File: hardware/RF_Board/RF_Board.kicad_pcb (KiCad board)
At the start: 4 copper layers, 90 x 90 mm, 127 parts, among them J1 Conn_Coaxial, J2 Conn_01x07_Male, J3 Conn_Coaxial, J4 Conn_01x07_Male, J5 Conn_01x06_Female, J6 Conn_01x06_Female, J7 Conn_01x06_Female, J9 LD15S33E4GX00LF, Q1 2N7002, Q2 2N7002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

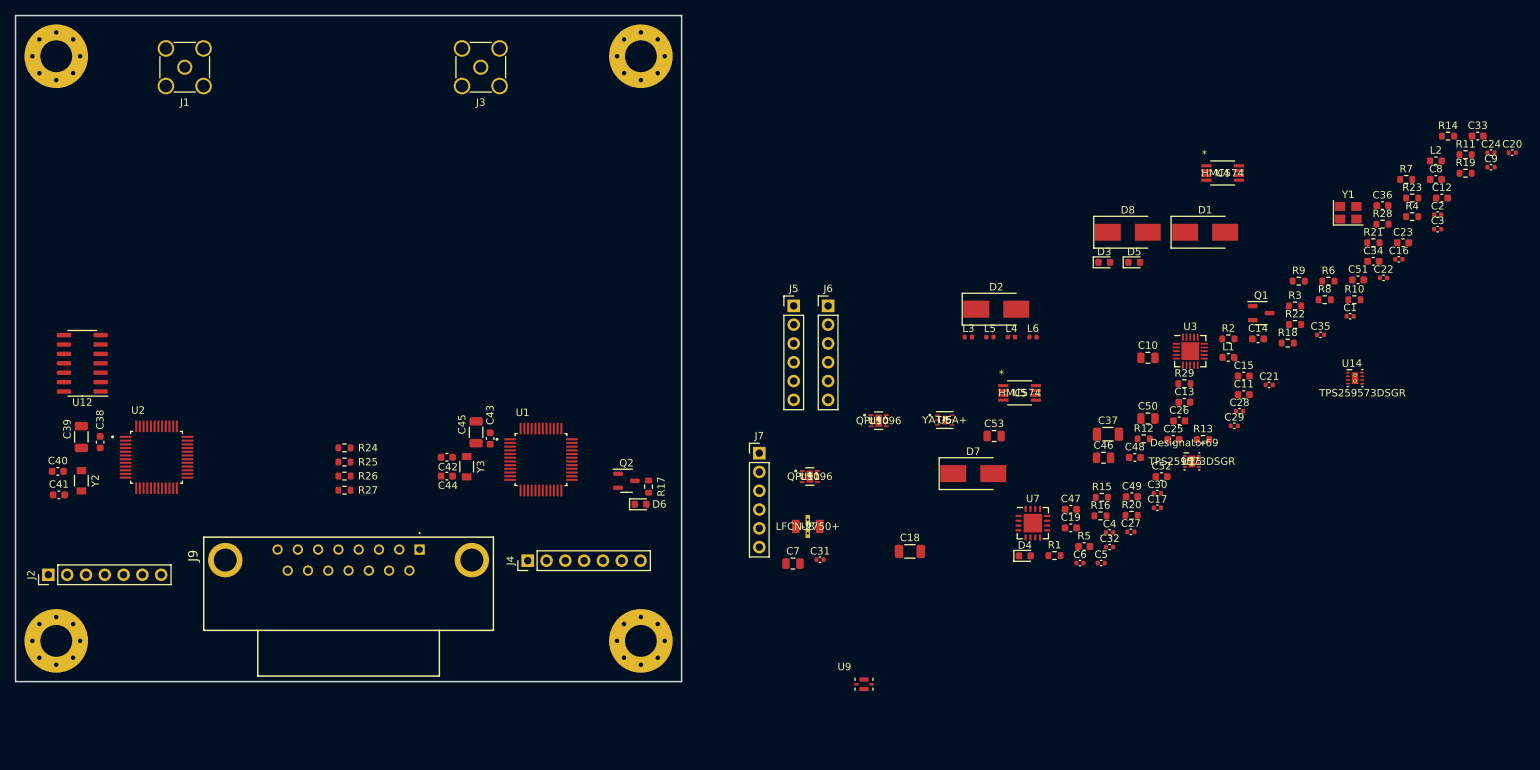
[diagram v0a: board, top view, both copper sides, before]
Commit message: RF board first draft placement
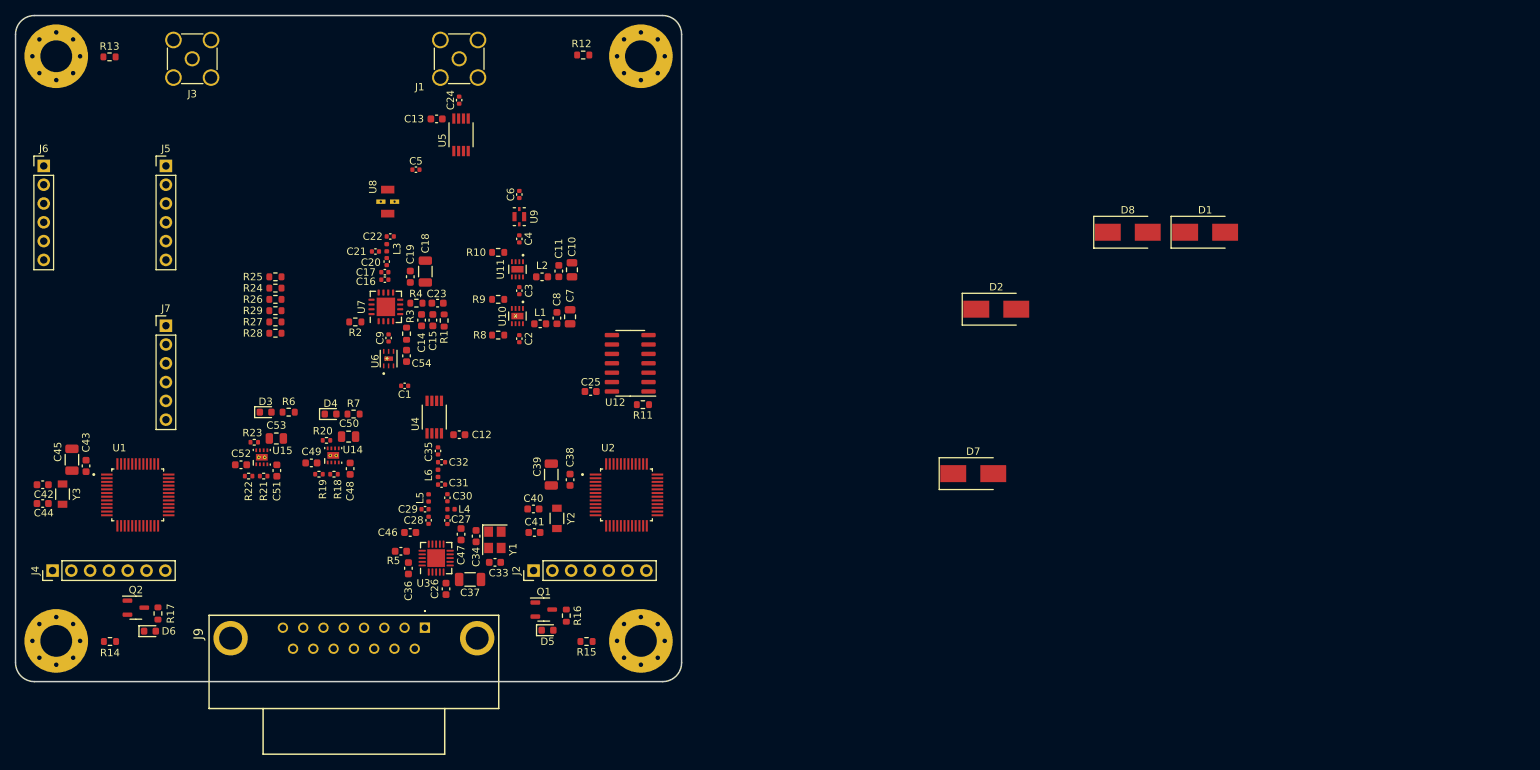
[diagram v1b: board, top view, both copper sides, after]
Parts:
- added C54: 100nF, RF_Board_Footprints:C_0603_1608Metric, F.Cu at (52.8, 46.0)
- C46: value 1uF -> 100nF; footprint RF_Board_Footprints:C_0805_2012Metric -> RF_Board_Footprints:C_0603_1608Metric
- R18, R19, R20, R21, R22, R23: footprint RF_Board_Footprints:R_0603_1608Metric -> RF_Board_Footprints:R_0402_1005Metric
- moved R14 193.3 mm to (12.8, 84.6)
- moved R19 160.2 mm to (41.0, 62.0), turned to 180 degrees
- moved R23 159.9 mm to (32.3, 57.7), turned to 180 degrees
- moved R13 156.5 mm to (12.7, 5.59)
- moved R21 153.2 mm to (33.5, 62.2), turned to 180 degrees
- moved C20 152.8 mm to (50.2, 33.2), turned to 90 degrees
- moved C9 150.7 mm to (50.4, 43.6), turned to 90 degrees
- moved R28 150.3 mm to (35.1, 42.9)
- moved C51 148.4 mm to (35.3, 61.5), turned to -90 degrees
- moved R7 145.7 mm to (45.7, 53.8)
- moved C33 144.7 mm to (64.8, 73.9), turned to 180 degrees
- moved R22 142.9 mm to (31.5, 62.2), turned to 180 degrees
- moved R6 141.6 mm to (36.9, 53.6)
- moved C36 140.5 mm to (53.1, 74.7), turned to -90 degrees
- moved C24 139.6 mm to (59.9, 11.4), turned to 90 degrees
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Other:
- outline, holes or cut-outs redrawn

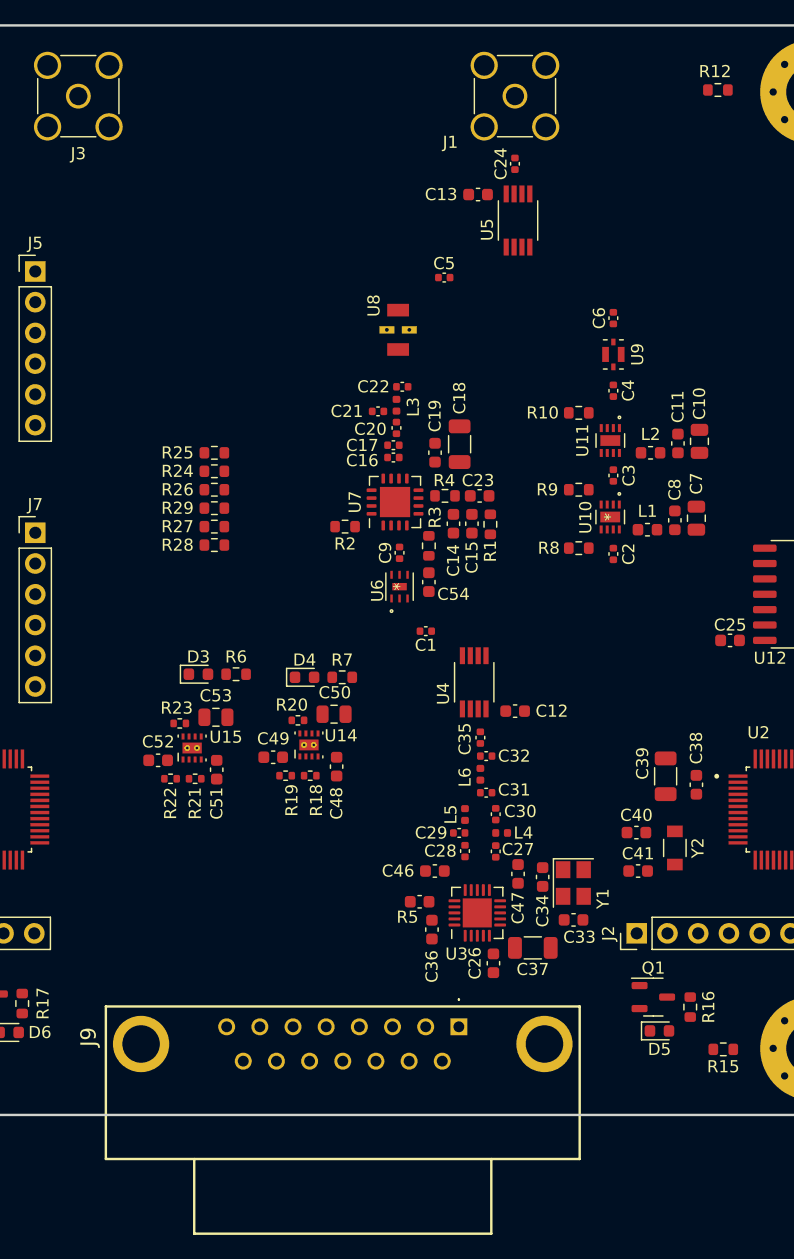
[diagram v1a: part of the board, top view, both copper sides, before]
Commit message: more RF board layout
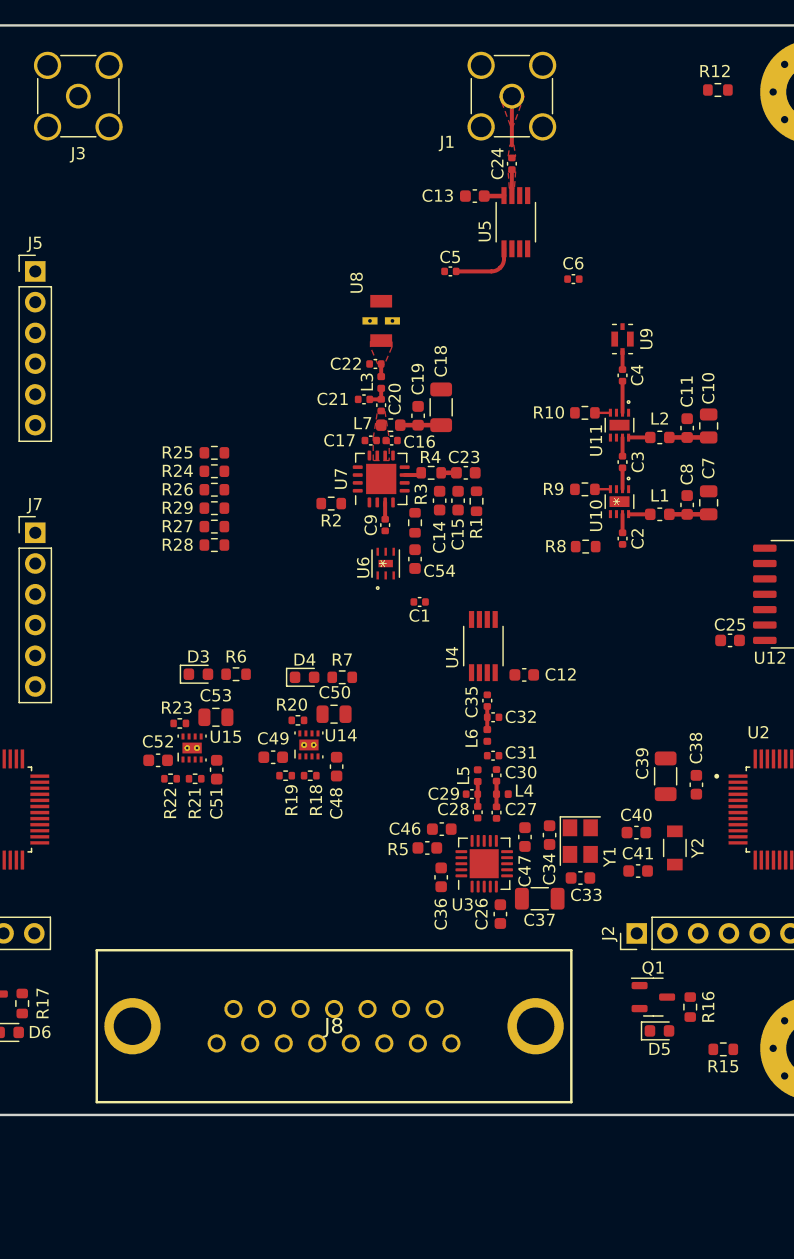
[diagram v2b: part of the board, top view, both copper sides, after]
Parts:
- removed J9: LD15S33E4GX00LF, RF_Board_Footprints:LD15S33E4GX00LF
- added J8: L77TSAH15SOL2RM8, RF_Board_Footprints:L77TSAH15SOL2RM8, F.Cu at (45.0, 81.2)
- added L7: 18nH, RF_Board_Footprints:L_0603_1608Metric, F.Cu at (49.7, 33.0)
- moved C6 4.61 mm to (64.8, 21.0), turned to 180 degrees
- moved R5 4.49 mm to (52.7, 67.9)
- moved C36 4.38 mm to (53.8, 70.4)
- moved C26 4.10 mm to (58.7, 73.4)
- moved C37 4.10 mm to (62.0, 72.1)
- moved U3 4.10 mm to (57.4, 69.2)
- moved C33 3.51 mm to (65.4, 70.4)
- moved C34 3.51 mm to (62.8, 66.9)
- moved Y1 3.51 mm to (65.3, 67.4)
- moved C46 3.51 mm to (53.9, 66.4)
- moved C18 3.41 mm to (53.8, 31.5)
- moved C28 3.37 mm to (56.9, 65.0)
- moved L5 3.37 mm to (56.9, 62.0)
- moved C29 3.37 mm to (56.4, 63.5)
- moved C19 3.35 mm to (51.9, 32.2)
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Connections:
- C16 pad 1: +5V -> Net-(C16-Pad1)
- C17 pad 1: +5V -> Net-(C16-Pad1)
- C20 pad 1: +5V -> Net-(C16-Pad1)
- U7 pad 10: +5V -> Net-(C16-Pad1)
- U7 pad 11: +5V -> Net-(C16-Pad1)
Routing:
- net +5V: track 0.00 -> 12.8 mm
- net Net-(C5-Pad2): track 0.00 -> 5.36 mm
- net Net-(C24-Pad2): track 0.00 -> 4.06 mm
- net Net-(C4-Pad1): track 0.00 -> 2.60 mm
- net Net-(C24-Pad1): track 0.00 -> 2.15 mm
- net Net-(C27-Pad2): track 0.00 -> 2.12 mm
- net Net-(C28-Pad2): track 0.00 -> 2.06 mm
- net Net-(C32-Pad2): track 0.00 -> 1.91 mm
- net Net-(C20-Pad2): track 0.00 -> 1.85 mm
- net Net-(L2-Pad2): track 0.00 -> 1.79 mm
- net Net-(C3-Pad1): track 0.00 -> 1.76 mm
- net Net-(L1-Pad2): track 0.00 -> 1.76 mm
- net Net-(C2-Pad2): track 0.00 -> 1.54 mm
- net Net-(C3-Pad2): track 0.00 -> 1.54 mm
- net Net-(C4-Pad2): track 0.00 -> 1.49 mm
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- added copper zone on In1.Cu, net GND
- added copper zone on F.Cu, net Net-(C16-Pad1)
- added copper zone on F.Cu, net Net-(C22-Pad2)
- added copper zone on F.Cu, net Net-(C24-Pad1)
- added copper zone on F.Cu, net Net-(C24-Pad2)

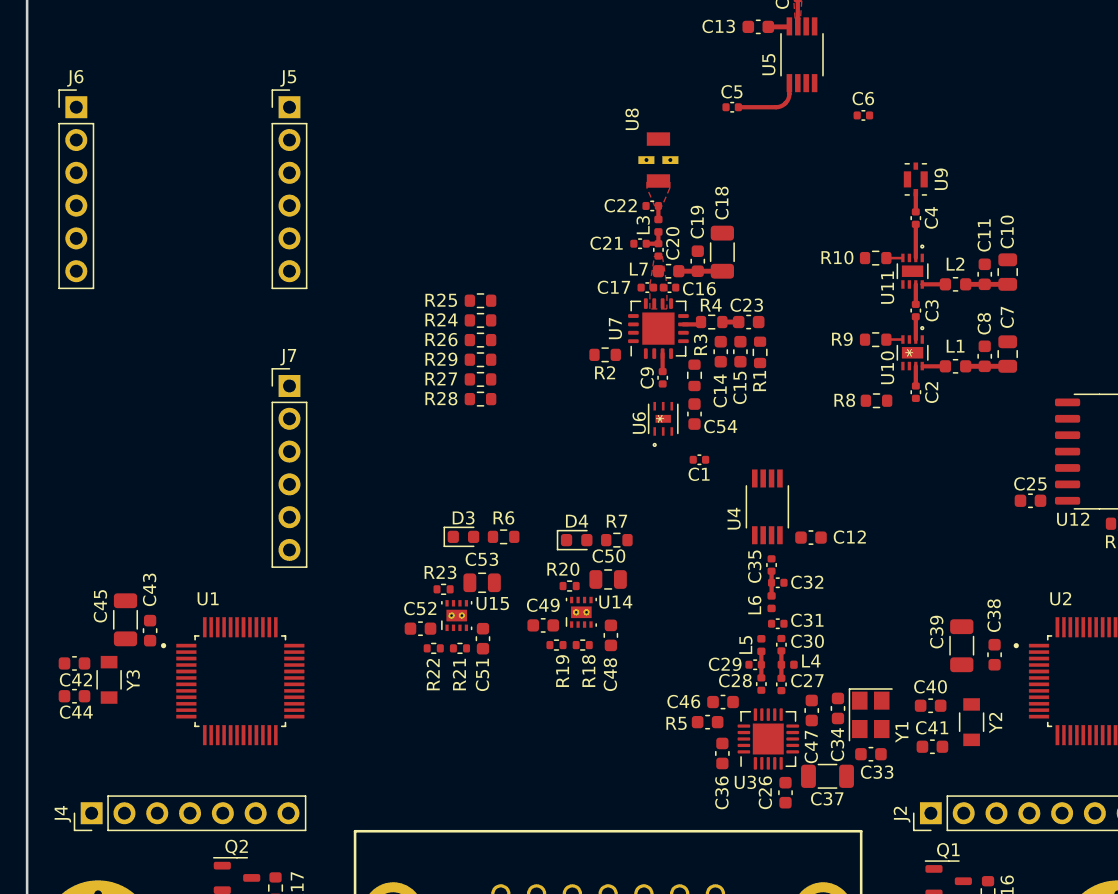
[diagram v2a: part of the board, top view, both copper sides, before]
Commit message: finished first pass of SBand chain
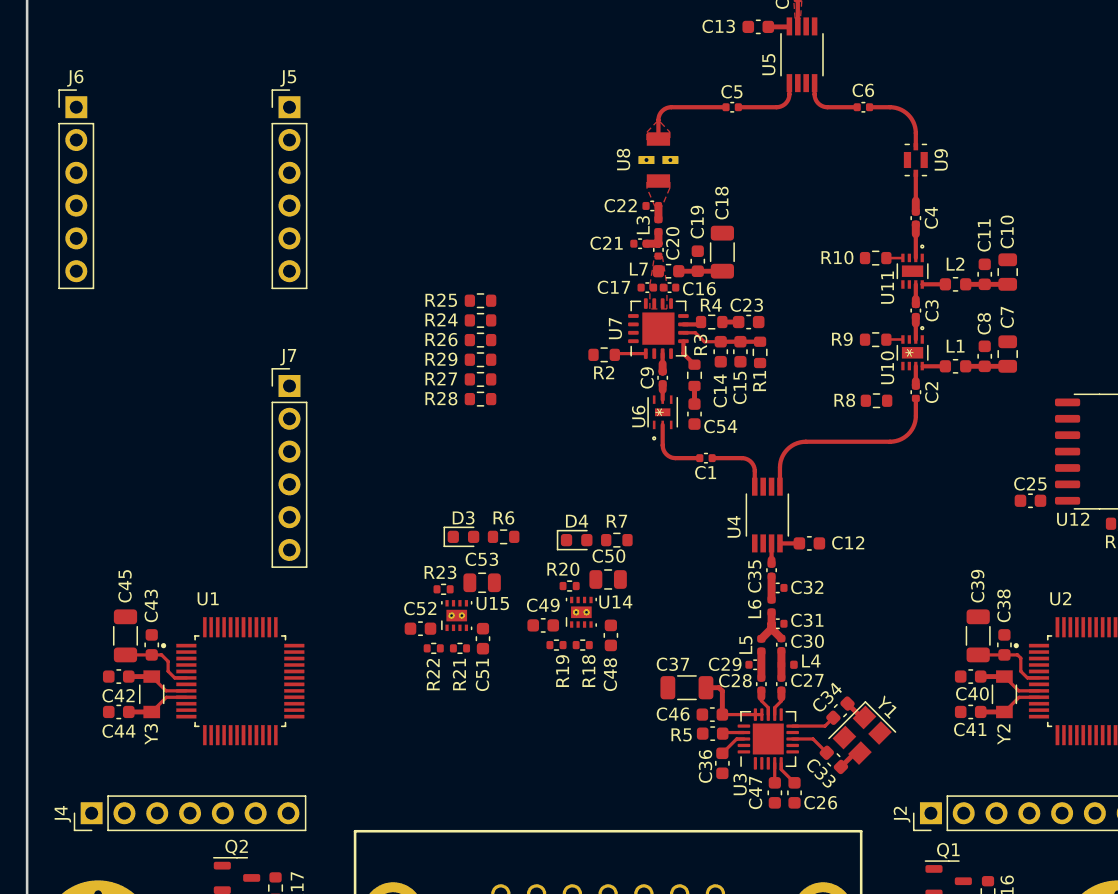
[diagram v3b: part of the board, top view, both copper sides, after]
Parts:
- moved C37 12.9 mm to (51.1, 65.3), turned to 0 degrees
- moved C47 6.99 mm to (57.9, 73.4), turned to -90 degrees
- moved C41 4.01 mm to (73.1, 67.2)
- moved C40 3.84 mm to (73.1, 64.4)
- moved C44 3.64 mm to (7.10, 67.2)
- moved C42 3.58 mm to (7.10, 64.4)
- moved Y3 3.49 mm to (9.65, 65.8)
- moved Y2 3.33 mm to (75.7, 65.8)
- moved C33 2.90 mm to (62.5, 70.9), turned to 135 degrees
- moved Y1 1.71 mm to (64.7, 69.0), turned to -135 degrees
- moved U9 1.50 mm to (68.8, 24.4)
- moved C39 1.48 mm to (73.7, 61.3)
- moved C46 1.27 mm to (53.1, 67.4)
- moved C45 1.24 mm to (7.62, 61.3)
- moved C43 1.11 mm to (9.65, 62.0)
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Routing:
- net +3.3V: track 0.00 -> 21.8 mm
- net Net-(C2-Pad1): track 0.00 -> 15.5 mm
- net Net-(C5-Pad1): track 0.00 -> 7.23 mm
- net /PA_VDET: track 0.00 -> 6.22 mm
- net Net-(C6-Pad1): track 0.00 -> 5.70 mm
- net Net-(C1-Pad1): track 0.00 -> 5.04 mm
- net /CC2500_XOUT: track 0.00 -> 4.98 mm
- net Net-(C1-Pad2): track 0.00 -> 4.98 mm
- net /CC2500_XIN: track 0.00 -> 4.97 mm
- net /RFM_XOUT: track 0.00 -> 4.93 mm
- net /RFM_XIN: track 0.00 -> 4.91 mm
- net Net-(C6-Pad2): track 0.00 -> 4.70 mm
- net Net-(C30-Pad2): track 0.00 -> 3.84 mm
- net Net-(C34-Pad2): track 0.00 -> 3.42 mm
- net Net-(C33-Pad2): track 0.00 -> 3.09 mm
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- added copper zone on F.Cu, net Net-(C5-Pad1)
